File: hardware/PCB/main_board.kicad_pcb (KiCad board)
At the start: 2 copper layers, 72 x 100 mm, 6 parts

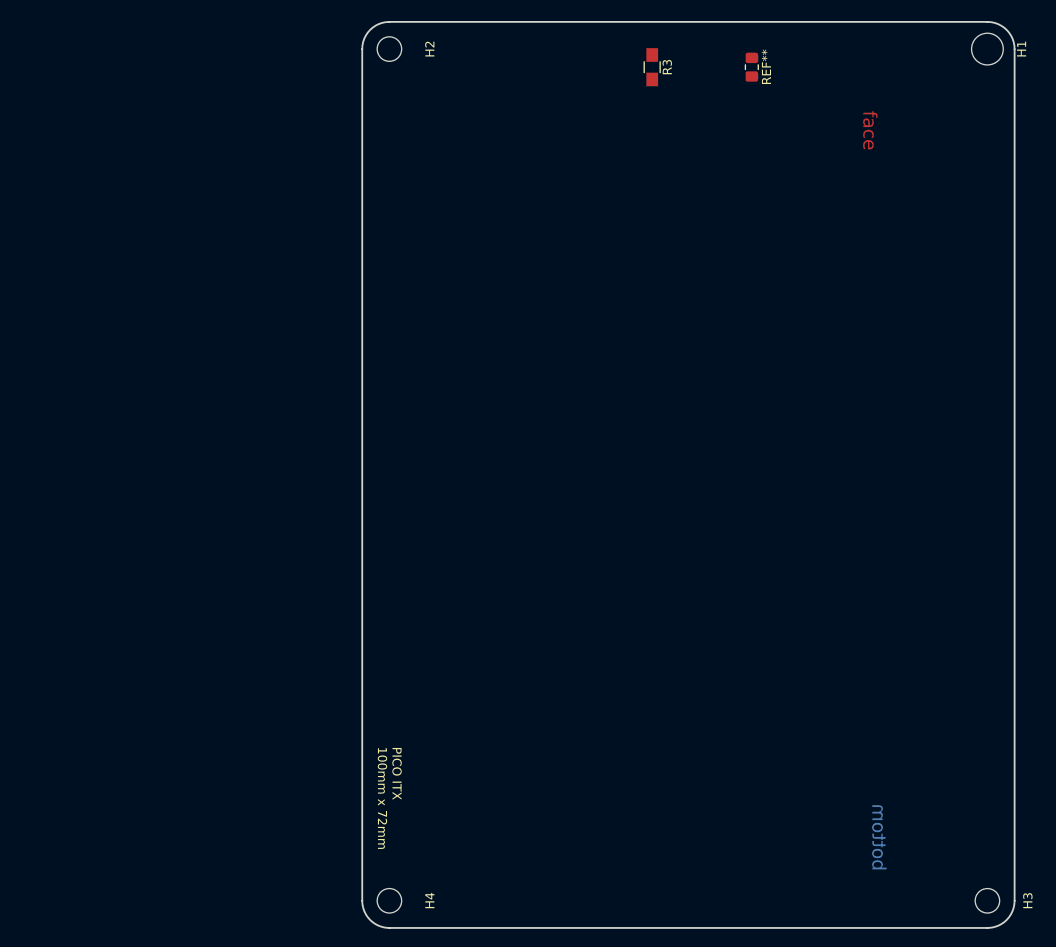
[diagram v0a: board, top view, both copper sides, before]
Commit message: update pcb screw hole position,
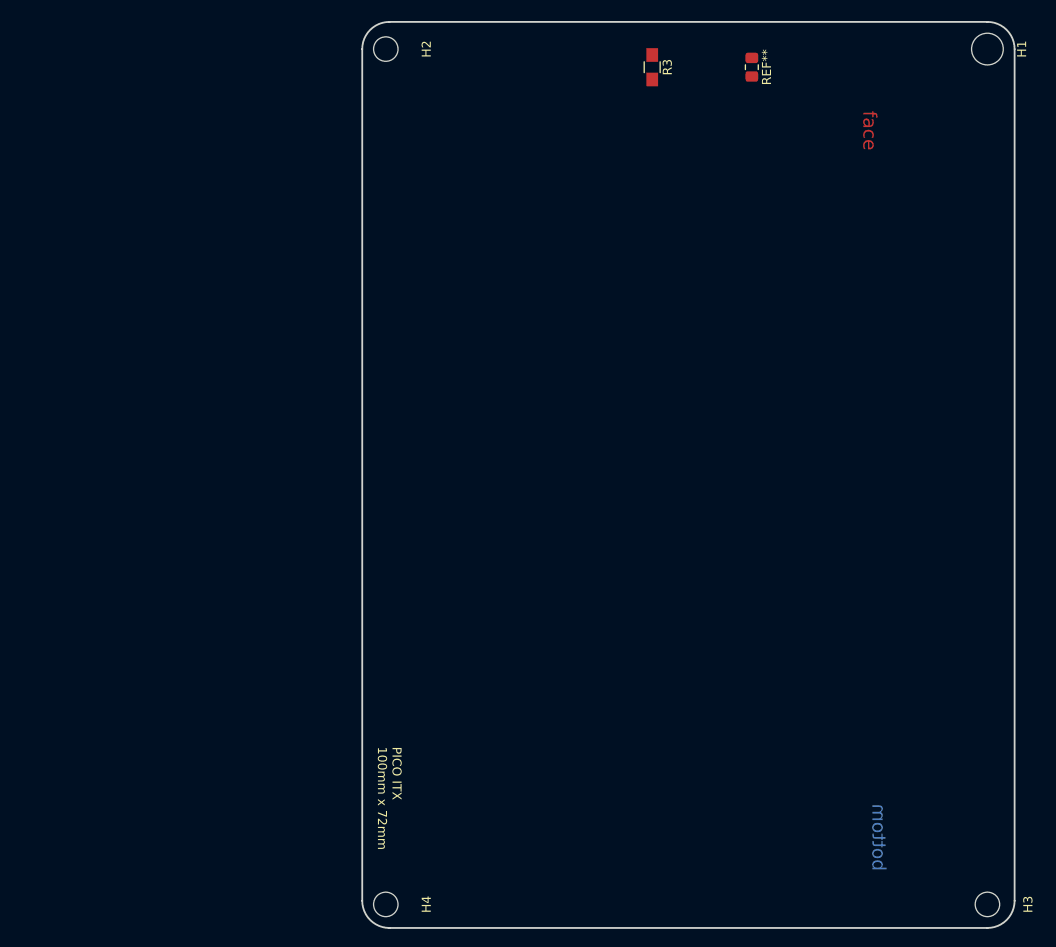
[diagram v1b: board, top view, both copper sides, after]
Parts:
- moved H4 0.57 mm to (17.8, 113.5)
- moved H2 0.40 mm to (17.8, 19.1)
- moved H3 0.40 mm to (84.2, 113.5)
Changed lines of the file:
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@@
     (mod_text_size 1 1)
     (mod_text_width 0.15)
-    (pad_size 7 7)
-    (pad_drill 3.5)
+    (pad_size 2.7 2.7)
+    (pad_drill 2.7)
     (pad_to_mask_clearance 0.051)
     (solder_mask_min_width 0.25)
@@
     )
   )
-  (module footprint-lib:MountingHole_3.5mm_M3,rpi_like (layer F.Cu)
+  (module footprint-lib:MountingHole_3.5mm_M3,rpi_like locked (layer F.Cu)
     (at 84.174493 19.065745 270)
     (descr "Mounting Hole 2.7mm, no annular, M2.5")
@@
       (solder_mask_margin 1.5) (clearance 1.5))
   )
-  (module footprint-lib:MountingHole_3.5mm_M3,rpi_like (layer F.Cu)
-    (at 18.174492 113.065745 270)
+  (module footprint-lib:MountingHole_3.5mm_M3,rpi_like locked (layer F.Cu)
+    (at 17.774493 113.465744 270)
     (descr "Mounting Hole 2.7mm, no annular, M2.5")
     (tags "mounting hole 2.7mm no annular m2.5")
@@
       (solder_mask_margin 1.5) (clearance 1.5))
   )
-  (module footprint-lib:MountingHole_3.5mm_M3,rpi_like (layer F.Cu)
-    (at 84.174492 113.065746 270)
+  (module footprint-lib:MountingHole_3.5mm_M3,rpi_like locked (layer F.Cu)
+    (at 84.174492 113.465744 270)
     (descr "Mounting Hole 2.7mm, no annular, M2.5")
     (tags "mounting hole 2.7mm no annular m2.5")
@@
       (solder_mask_margin 1.5) (clearance 1.5))
   )
-  (module footprint-lib:MountingHole_3.5mm_M3,rpi_like (layer F.Cu)
-    (at 18.174492 19.065744 270)
+  (module footprint-lib:MountingHole_3.5mm_M3,rpi_like locked (layer F.Cu)
+    (at 17.774493 19.065744 270)
     (descr "Mounting Hole 2.7mm, no annular, M2.5")
     (tags "mounting hole 2.7mm no annular m2.5")
@@
     (arrow2b (pts (xy 2 116) (xy 1.413579 114.873496)))
   )
-  (dimension 94.000001 (width 0.12) (layer F.SilkS)
-    (gr_text "94.000 mm" (at 6.73 66.065744 270) (layer F.SilkS)
-      (effects (font (size 1 1) (thickness 0.15)))
-    )
-    (feature1 (pts (xy 18.174492 113.065745) (xy 7.413579 113.065745)))
+  (dimension 94.4 (width 0.12) (layer F.SilkS)
+    (gr_text "94.400 mm" (at 6.73 66.265744 270) (layer F.SilkS)
+      (effects (font (size 1 1) (thickness 0.15)))
+    )
+    (feature1 (pts (xy 18.174492 113.465744) (xy 7.413579 113.465744)))
     (feature2 (pts (xy 18.174492 19.065744) (xy 7.413579 19.065744)))
-    (crossbar (pts (xy 8 19.065744) (xy 8 113.065745)))
-    (arrow1a (pts (xy 8 113.065745) (xy 7.413579 111.939241)))
-    (arrow1b (pts (xy 8 113.065745) (xy 8.586421 111.939241)))
+    (crossbar (pts (xy 8 19.065744) (xy 8 113.465744)))
+    (arrow1a (pts (xy 8 113.465744) (xy 7.413579 112.33924)))
+    (arrow1b (pts (xy 8 113.465744) (xy 8.586421 112.33924)))
     (arrow2a (pts (xy 8 19.065744) (xy 7.413579 20.192248)))
     (arrow2b (pts (xy 8 19.065744) (xy 8.586421 20.192248)))
@@
     (arrow2b (pts (xy 87 6) (xy 85.873496 6.586421)))
   )
-  (dimension 66.000001 (width 0.12) (layer F.SilkS)
-    (gr_text "66.000 mm" (at 51.174492 9.73 -8.681178542e-07) (layer F.SilkS)
-      (effects (font (size 1 1) (thickness 0.15)))
-    )
-    (feature1 (pts (xy 18.174492 19.065744) (xy 18.174492 10.413579)))
-    (feature2 (pts (xy 84.174493 19.065745) (xy 84.174493 10.41358)))
-    (crossbar (pts (xy 84.174493 11.000001) (xy 18.174492 11)))
-    (arrow1a (pts (xy 18.174492 11) (xy 19.300996 10.413579)))
-    (arrow1b (pts (xy 18.174492 11) (xy 19.300996 11.586421)))
-    (arrow2a (pts (xy 84.174493 11.000001) (xy 83.047989 10.41358)))
-    (arrow2b (pts (xy 84.174493 11.000001) (xy 83.047989 11.586422)))
+  (dimension 66.4 (width 0.12) (layer F.SilkS)
+    (gr_text "66.400 mm" (at 50.974493 10.795744 -8.62888237e-07) (layer F.SilkS)
+      (effects (font (size 1 1) (thickness 0.15)))
+    )
+    (feature1 (pts (xy 17.774493 19.065744) (xy 17.774493 11.479323)))
+    (feature2 (pts (xy 84.174493 19.065745) (xy 84.174493 11.479324)))
+    (crossbar (pts (xy 84.174493 12.065745) (xy 17.774493 12.065744)))
+    (arrow1a (pts (xy 17.774493 12.065744) (xy 18.900997 11.479323)))
+    (arrow1b (pts (xy 17.774493 12.065744) (xy 18.900997 12.652165)))
+    (arrow2a (pts (xy 84.174493 12.065745) (xy 83.047989 11.479324)))
+    (arrow2b (pts (xy 84.174493 12.065745) (xy 83.047989 12.652166)))
   )
   (gr_text bottom (at 72.174493 106.065742 -90) (layer B.Cu)

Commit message: update,
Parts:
- removed REF**: C_0805_2012Metric_Pad1.15x1.40mm_HandSolder, Capacitor_SMD:C_0805_2012Metric_Pad1.15x1.40mm_HandSolder
- added AE1: Antenna_Shield, footprint-lib:rainsun-AN9520, F.Cu at (36.8, 20.1)
- added BZ1: BUZZER,MLT-8530, footprint-lib:MLT-8530, F.Cu at (59.3, 22.5)
- added C1: CP47uf,10V, Capacitor_SMD:CP_Elec_4x5.3, F.Cu at (82.1, 38.2)
- added C2: CP47uf,10V, Capacitor_SMD:CP_Elec_4x5.3, F.Cu at (82.3, 32.7)
- added D2: LED_GREEN,0805, footprint-lib:LED_0805_2012Metric, F.Cu at (34.6, 63.9)
- added J1: TTL_UART, Connector_PinHeader_2.54mm:PinHeader_1x04_P2.54mm_Vertical, F.Cu at (83.6, 77.2)
- added J10: POWER, Connector_PinHeader_2.54mm:PinHeader_1x04_P2.54mm_Vertical, F.Cu at (69.7, 95.0)
- added J11: SDC_DEBUG, Connector_PinHeader_2.54mm:PinHeader_1x06_P2.54mm_Vertical, F.Cu at (43.8, 46.1)
- added J12: UART_DEBUG, Connector_PinHeader_2.54mm:PinHeader_1x03_P2.54mm_Vertical, F.Cu at (46.2, 27.0)
- added J2: DPS1_UART, Connector_PinHeader_2.54mm:PinHeader_1x04_P2.54mm_Vertical, F.Cu at (20.2, 38.7)
- added J3: DPS2_UART, Connector_PinHeader_2.54mm:PinHeader_1x04_P2.54mm_Vertical, F.Cu at (19.8, 25.1)
- added J4: PE_IO_0, Connector_PinHeader_2.54mm:PinHeader_1x04_P2.54mm_Vertical, F.Cu at (56.7, 94.7)
- added J5: PE_IO_1, Connector_PinHeader_2.54mm:PinHeader_1x04_P2.54mm_Vertical, F.Cu at (51.7, 94.7)
- added J6: PE_IO_2, Connector_PinHeader_2.54mm:PinHeader_1x04_P2.54mm_Vertical, F.Cu at (46.6, 94.6)
- added J7: PE_IO_3/TWI0, Connector_PinHeader_2.54mm:PinHeader_1x04_P2.54mm_Vertical, F.Cu at (40.3, 94.6)
- added J8: PA_IO, Connector_PinHeader_2.54mm:PinHeader_1x04_P2.54mm_Vertical, F.Cu at (34.6, 94.6)
- added J9: USB_IO, Connector_PinHeader_2.54mm:PinHeader_1x04_P2.54mm_Vertical, F.Cu at (61.8, 95.0)
- added JP1: Jumper, Jumper:SolderJumper-2_P1.3mm_Open_TrianglePad1.0x1.5mm, F.Cu at (75.6, 26.5)
- added Q1: 2N3904(1AM), footprint-lib:MBT3904_1AM_SOT, F.Cu at (-21.3, 76.5)
- added R1: R470,0603, Resistor_SMD:R_0603_1608Metric_Pad1.05x0.95mm_HandSolder, F.Cu at (-21.4, 80.1)
- added R2: R103,0805, Resistor_SMD:R_0805_2012Metric_Pad1.15x1.40mm_HandSolder, F.Cu at (34.4, 68.2)
- added R4: R103,0603, Resistor_SMD:R_0603_1608Metric_Pad1.05x0.95mm_HandSolder, F.Cu at (27.2, 102.4)
- added R5: R103,0603, Resistor_SMD:R_0603_1608Metric_Pad1.05x0.95mm_HandSolder, F.Cu at (36.2, 102.1)
- added R6: R103,0603, Resistor_SMD:R_0603_1608Metric_Pad1.05x0.95mm_HandSolder, F.Cu at (46.6, 102.1)
- added R7: R103,0603, Resistor_SMD:R_0603_1608Metric_Pad1.05x0.95mm_HandSolder, F.Cu at (63.3, 101.8)
- added SW1: FEL, footprint-lib:SW_SPST_PTS645, F.Cu at (75.1, 108.9)
- added SW2: SW_Push, footprint-lib:SW_SPST_PTS645, F.Cu at (27.2, 109.3)
- added SW3: SW_Push, footprint-lib:SW_SPST_PTS645, F.Cu at (36.5, 109.1)
- added SW4: SW_Push, footprint-lib:SW_SPST_PTS645, F.Cu at (46.4, 108.9)
- added SW5: RESET, footprint-lib:SW_SPST_PTS645, F.Cu at (63.1, 108.7)
- added TP1: TestPoint, TestPoint:TestPoint_Keystone_5000-5004_Miniature, F.Cu at (75.5, 21.5)
- added U1: TTL_USB_CONVERTER, footprint-lib:TTL_USB_CONVERTER, F.Cu at (20.9, 83.6)
- added U10: RTL8723BS, footprint-lib:RL-SM02BD(RTL8723BS), F.Cu at (36.9, 31.6)
- added U11: 100KΩ,(1003),±1%,0603,C25803, w_smd_resistors:r_0603, F.Cu at (46.3, 35.3)
- added U12: 10KΩ,(1002),±1%,0603,C25804, w_smd_resistors:r_0603, F.Cu at (46.3, 38.9)
- added U13: M1,GPP,SMA,DO-214AC,C123825, footprint-lib:DO-214AC, F.Cu at (67.8, 22.7)
- added U2: LICHEEPI_NANO, footprint-lib:licheepi_nano, F.Cu at (72.7, 57.4)
- added U3: 47KΩ,(4702),±1%,0603,C25819, w_smd_resistors:r_0603, F.Cu at (41.3, 42.9)
- added U4: 47KΩ,(4702),±1%,0603,C25819, w_smd_resistors:r_0603, F.Cu at (43.9, 42.7)
- added U5: 47KΩ,(4702),±1%,0603,C25819, w_smd_resistors:r_0603, F.Cu at (31.2, 42.7)
- added U6: 47KΩ,(4702),±1%,0603,C25819, w_smd_resistors:r_0603, F.Cu at (33.9, 42.6)
- added U7: 47KΩ,(4702),±1%,0603,C25819, w_smd_resistors:r_0603, F.Cu at (36.2, 42.7)
- added U8: 33pF,(330),±5%,50V,C0G,0603,C1663, w_smd_cap:c_0603, F.Cu at (30.9, 23.8)
- added U9: 100KΩ,(1003),±1%,0603,C25803, w_smd_resistors:r_0603, F.Cu at (46.4, 37.1)
- R3: value 331 -> R103,0603; footprint footprint-lib:R_0805_HandSoldering -> Resistor_SMD:R_0603_1608Metric_Pad1.05x0.95mm_HandSolder
- moved R3 85.4 mm to (75.1, 101.8), turned to 0 degrees
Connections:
- R3 pad 1: (no net) -> Net-(R3-Pad1)
- R3 pad 2: (no net) -> GND

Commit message: all components in the board,
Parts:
- moved R1 107.8 mm to (72.2, 26.6), turned to 90 degrees
- moved Q1 100.2 mm to (68.3, 31.8)
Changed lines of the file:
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@@
   )
   (module Resistor_SMD:R_0603_1608Metric_Pad1.05x0.95mm_HandSolder (layer F.Cu)
-    (at -21.395 80.075)
+    (at 72.2376 26.5544 90)
     (descr "Resistor SMD 0603 (1608 Metric), square (rectangular) end terminal, IPC_7351 nominal with elongated pad for handsoldering. (Body size source: http://www.tortai-tech.com/upload/download/2011102023233369053.pdf), generated with kicad-footprint-generator")
     (tags "resistor handsolder")
     (attr smd)
-    (fp_text reference R1 (at 0 -1.43) (layer F.SilkS)
+    (fp_text reference R1 (at 0 -1.43 90) (layer F.SilkS)
       (effects (font (size 1 1) (thickness 0.15)))
     )
-    (fp_text value R470,0603 (at 0 1.43) (layer F.Fab)
+    (fp_text value R470,0603 (at 0 1.43 90) (layer F.Fab)
       (effects (font (size 1 1) (thickness 0.15)))
     )
-    (fp_text user %R (at 0 0) (layer F.Fab)
+    (fp_text user %R (at 0 0 90) (layer F.Fab)
       (effects (font (size 0.4 0.4) (thickness 0.06)))
     )
@@
     (fp_line (start -0.8 -0.4) (end 0.8 -0.4) (layer F.Fab) (width 0.1))
     (fp_line (start -0.8 0.4) (end -0.8 -0.4) (layer F.Fab) (width 0.1))
-    (pad 2 smd roundrect (at 0.875 0) (size 1.05 0.95) (layers F.Cu F.Paste F.Mask) (roundrect_rratio 0.25)
+    (pad 2 smd roundrect (at 0.875 0 90) (size 1.05 0.95) (layers F.Cu F.Paste F.Mask) (roundrect_rratio 0.25)
       (net 22 "Net-(JP1-Pad2)"))
-    (pad 1 smd roundrect (at -0.875 0) (size 1.05 0.95) (layers F.Cu F.Paste F.Mask) (roundrect_rratio 0.25)
+    (pad 1 smd roundrect (at -0.875 0 90) (size 1.05 0.95) (layers F.Cu F.Paste F.Mask) (roundrect_rratio 0.25)
       (net 23 "Net-(Q1-Pad1)"))
     (model ${KISYS3DMOD}/Resistor_SMD.3dshapes/R_0603_1608Metric.wrl
@@
   )
   (module footprint-lib:MBT3904_1AM_SOT (layer F.Cu)
-    (at -21.345 76.545)
+    (at 68.326 31.8008)
     (descr "SOT-23, Standard")
     (tags MBT3904_1AM_SOT)
